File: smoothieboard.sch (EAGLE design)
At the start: 237 parts, among them IC1 LPC1769, IC10 LM1117-3.3V, IC11 78L12F, IC2 A4982, IC3 A4982, IC4 MCP44X1, IC5 A4982, IC6 A4982, J10 POWER_JACKSMD, J5 POWER_JACKSMD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

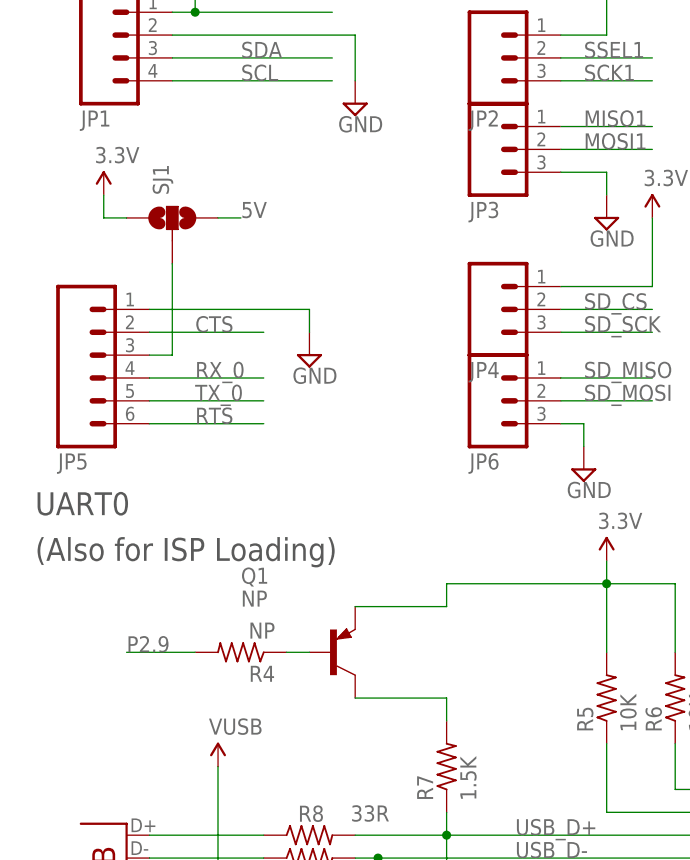
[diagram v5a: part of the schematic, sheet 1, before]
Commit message: switch USB CONNECT transistor for a FET, move UART voltage selector next to UART header
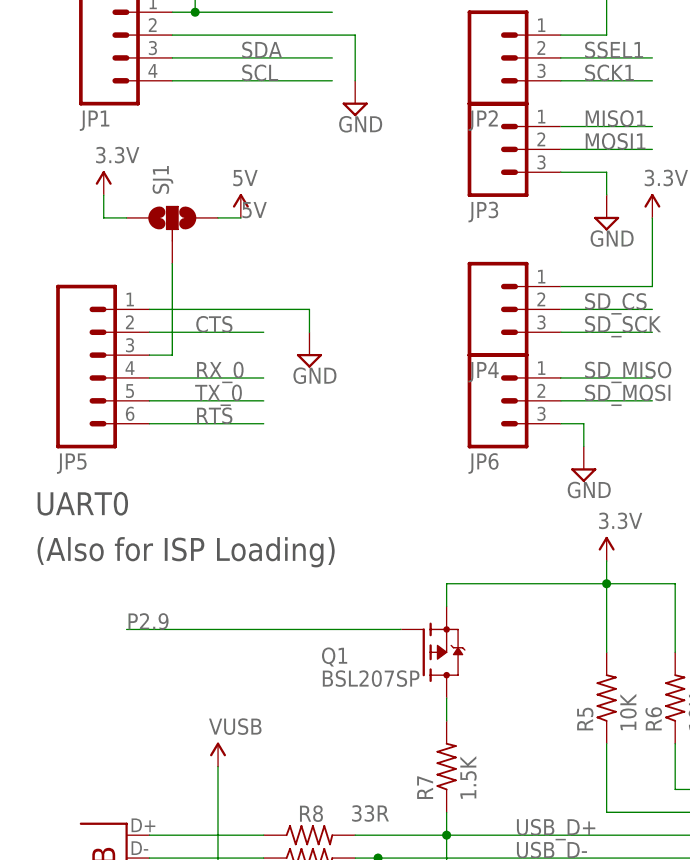
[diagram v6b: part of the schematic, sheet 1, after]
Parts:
- removed R4: NP, resistor:R-US_R0603
- Q1: value NP -> BSL207SP; device transistor-pnp:BC857ALT1SMD -> transistor-fet:BSL207SP
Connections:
- removed net N$59: Q1.B, R4.1
- net 3.3V: now also Q1.S; no longer Q1.E
- net N$51: now also Q1.D; no longer Q1.C
- net P2.9: now also Q1.G; no longer R4.2
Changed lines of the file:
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@@
 <part name="R57" library="resistor" deviceset="R-US_" device="R0603" value="49.9R"/>
 <part name="JP20" library="SparkFun" deviceset="M03" device="PTH"/>
-<part name="Q1" library="transistor-pnp" deviceset="BC857*" device="SMD" technology="ALT1" value="NP"/>
-<part name="R4" library="resistor" deviceset="R-US_" device="R0603" value="NP"/>
 <part name="JP13" library="SparkFun" deviceset="M04" device="1X04_NO_SILK"/>
 <part name="SUPPLY71" library="supply2" deviceset="GND" device=""/>
@@
 <part name="SJ1" library="SparkFun" deviceset="SOLDERJUMPER_2WAY" device="S"/>
 <part name="P+23" library="SparkFun" deviceset="3.3V" device=""/>
+<part name="Q1" library="transistor-fet" deviceset="BSL207SP" device=""/>
+<part name="U$3" library="SparkFun" deviceset="5V" device=""/>
+<part name="U$4" library="SparkFun" deviceset="5V" device=""/>
 </parts>
 <sheets>
@@
 <instance part="SUPPLY36" gate="GND" x="73.66" y="193.04"/>
 <instance part="JP20" gate="G$1" x="378.46" y="88.9" rot="R180"/>
-<instance part="Q1" gate="G$1" x="45.72" y="172.72"/>
-<instance part="R4" gate="G$1" x="35.56" y="172.72" rot="R180"/>
 <instance part="JP13" gate="G$1" x="375.92" y="132.08" rot="R180"/>
 <instance part="SUPPLY74" gate="GND" x="281.94" y="119.38" rot="R270"/>
@@
 <instance part="SJ1" gate="G$1" x="27.94" y="220.98" rot="R90"/>
 <instance part="P+23" gate="G$1" x="20.32" y="223.52"/>
+<instance part="Q1" gate="G$1" x="55.88" y="172.72"/>
+<instance part="U$4" gate="G$1" x="35.56" y="220.98"/>
 </instances>
 <busses>
@@
 <pinref part="P+30" gate="G$1" pin="3.3V"/>
 <pinref part="R6" gate="G$1" pin="2"/>
-<pinref part="Q1" gate="G$1" pin="E"/>
 <wire x1="58.42" y1="177.8" x2="58.42" y2="180.34" width="0.1524" layer="91"/>
 <wire x1="58.42" y1="180.34" x2="76.2" y2="180.34" width="0.1524" layer="91"/>
-<wire x1="58.42" y1="177.8" x2="48.26" y2="177.8" width="0.1524" layer="91"/>
+<pinref part="Q1" gate="G$1" pin="S"/>
 </segment>
 <segment>
@@
 </segment>
 <segment>
-<pinref part="SJ1" gate="G$1" pin="1"/>
 <pinref part="P+23" gate="G$1" pin="3.3V"/>
-<wire x1="22.86" y1="220.98" x2="20.32" y2="220.98" width="0.1524" layer="91"/>
 <wire x1="20.32" y1="220.98" x2="20.32" y2="223.52" width="0.1524" layer="91"/>
+<pinref part="SJ1" gate="G$1" pin="1"/>
+<wire x1="20.32" y1="220.98" x2="22.86" y2="220.98" width="0.1524" layer="91"/>
 </segment>
 </net>
@@
 </segment>
 <segment>
-<pinref part="R4" gate="G$1" pin="2"/>
-<wire x1="30.48" y1="172.72" x2="22.86" y2="172.72" width="0.1524" layer="91"/>
-<label x="22.86" y="172.72" size="1.778" layer="95"/>
+<wire x1="53.34" y1="175.26" x2="22.86" y2="175.26" width="0.1524" layer="91"/>
+<label x="22.86" y="175.26" size="1.778" layer="95"/>
+<pinref part="Q1" gate="G$1" pin="G"/>
 </segment>
 </net>
@@
 <net name="5V" class="0">
 <segment>
+<pinref part="U$4" gate="G$1" pin="5V"/>
+<pinref part="SJ1" gate="G$1" pin="3"/>
 <wire x1="33.02" y1="220.98" x2="35.56" y2="220.98" width="0.1524" layer="91"/>
 <label x="35.56" y="220.98" size="1.778" layer="95"/>
-<pinref part="SJ1" gate="G$1" pin="3"/>
 </segment>
 </net>
 <net name="N$51" class="0">
 <segment>
-<pinref part="Q1" gate="G$1" pin="C"/>
 <pinref part="R7" gate="G$1" pin="2"/>
 <wire x1="58.42" y1="167.64" x2="58.42" y2="165.1" width="0.1524" layer="91"/>
-<wire x1="58.42" y1="167.64" x2="48.26" y2="167.64" width="0.1524" layer="91"/>
-</segment>
-</net>
-<net name="N$59" class="0">
-<segment>
-<pinref part="Q1" gate="G$1" pin="B"/>
-<pinref part="R4" gate="G$1" pin="1"/>
-<wire x1="40.64" y1="172.72" x2="43.18" y2="172.72" width="0.1524" layer="91"/>
+<pinref part="Q1" gate="G$1" pin="D"/>
 </segment>
 </net>
@@
 <segment>
 <pinref part="JP5" gate="G$1" pin="3"/>
-<pinref part="SJ1" gate="G$1" pin="2"/>
 <wire x1="25.4" y1="205.74" x2="27.94" y2="205.74" width="0.1524" layer="91"/>
 <wire x1="27.94" y1="205.74" x2="27.94" y2="215.9" width="0.1524" layer="91"/>
+<pinref part="SJ1" gate="G$1" pin="2"/>
 </segment>
 </net>
@@
 <instance part="U$2" gate="B" x="162.56" y="86.36"/>
 <instance part="IC11" gate="G$1" x="170.18" y="142.24"/>
+<instance part="U$3" gate="G$1" x="43.18" y="38.1"/>
 </instances>
 <busses>
@@
 <segment>
 <wire x1="35.56" y1="48.26" x2="35.56" y2="38.1" width="0.1524" layer="91"/>
-<wire x1="35.56" y1="38.1" x2="45.72" y2="38.1" width="0.1524" layer="91"/>
+<wire x1="35.56" y1="38.1" x2="43.18" y2="38.1" width="0.1524" layer="91"/>
+<wire x1="43.18" y1="38.1" x2="45.72" y2="38.1" width="0.1524" layer="91"/>
 <wire x1="35.56" y1="33.02" x2="35.56" y2="38.1" width="0.1524" layer="91"/>
 <wire x1="33.02" y1="38.1" x2="35.56" y2="38.1" width="0.1524" layer="91"/>
@@
 <pinref part="D1" gate="G$1" pin="C"/>
 <pinref part="D2" gate="G$1" pin="C"/>
+<pinref part="U$3" gate="G$1" pin="5V"/>
+<junction x="43.18" y="38.1"/>
 </segment>
 </net>

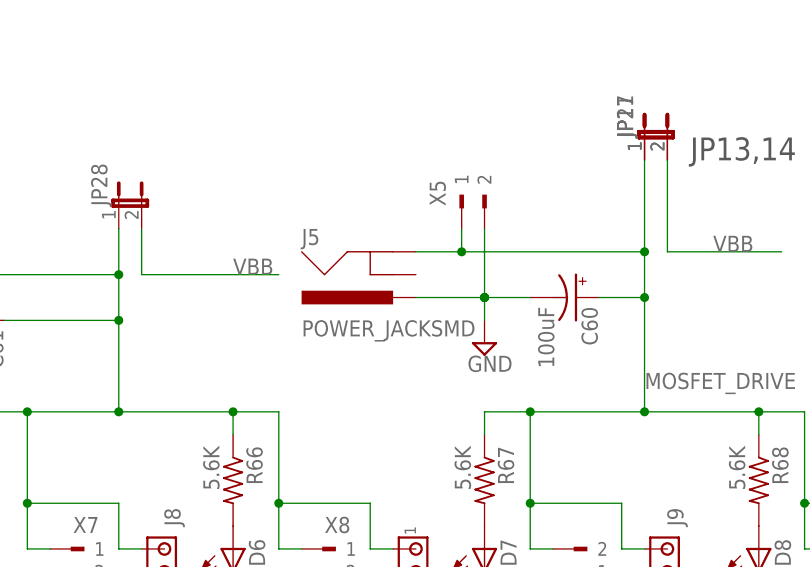
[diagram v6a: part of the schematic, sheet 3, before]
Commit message: Removed Mosfet Driver Power SMD Jack
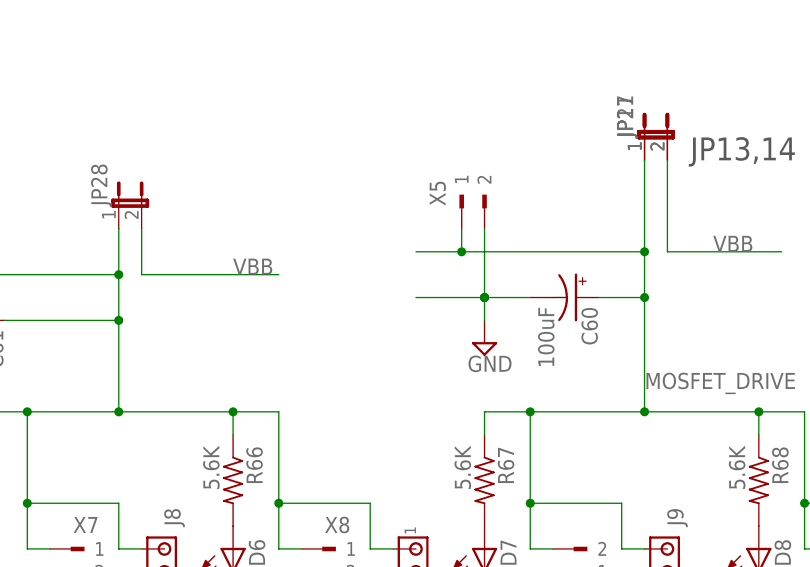
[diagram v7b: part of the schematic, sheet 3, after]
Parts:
- removed J5: POWER_JACKSMD, SparkFun:POWER_JACKSMD
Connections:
- net GND: no longer J5.PWR
- net MOSFET_DRIVE: no longer J5.GND
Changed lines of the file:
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@@
 <grid distance="0.1" unitdist="inch" unit="inch" style="lines" multiple="1" display="no" altdistance="0.01" altunitdist="inch" altunit="inch"/>
 <layers>
-<layer number="1" name="Top" color="4" fill="1" visible="yes" active="no"/>
-<layer number="2" name="Route2" color="2" fill="1" visible="yes" active="no"/>
-<layer number="3" name="Route3" color="4" fill="3" visible="yes" active="no"/>
-<layer number="4" name="Route4" color="1" fill="4" visible="yes" active="no"/>
-<layer number="5" name="Route5" color="4" fill="4" visible="yes" active="no"/>
-<layer number="6" name="Route6" color="1" fill="8" visible="yes" active="no"/>
-<layer number="7" name="Route7" color="4" fill="8" visible="yes" active="no"/>
-<layer number="8" name="Route8" color="1" fill="2" visible="yes" active="no"/>
-<layer number="9" name="Route9" color="4" fill="2" visible="yes" active="no"/>
-<layer number="10" name="Route10" color="1" fill="7" visible="yes" active="no"/>
-<layer number="11" name="Route11" color="4" fill="7" visible="yes" active="no"/>
-<layer number="12" name="Route12" color="1" fill="5" visible="yes" active="no"/>
-<layer number="13" name="Route13" color="4" fill="5" visible="yes" active="no"/>
-<layer number="14" name="Route14" color="1" fill="6" visible="yes" active="no"/>
-<layer number="15" name="Route15" color="5" fill="1" visible="yes" active="no"/>
-<layer number="16" name="Bottom" color="1" fill="1" visible="yes" active="no"/>
-<layer number="17" name="Pads" color="2" fill="1" visible="yes" active="no"/>
-<layer number="18" name="Vias" color="2" fill="1" visible="yes" active="no"/>
-<layer number="19" name="Unrouted" color="6" fill="1" visible="yes" active="no"/>
-<layer number="20" name="Dimension" color="15" fill="1" visible="yes" active="no"/>
-<layer number="21" name="tPlace" color="7" fill="1" visible="yes" active="no"/>
-<layer number="22" name="bPlace" color="7" fill="1" visible="yes" active="no"/>
-<layer number="23" name="tOrigins" color="15" fill="1" visible="yes" active="no"/>
-<layer number="24" name="bOrigins" color="15" fill="1" visible="yes" active="no"/>
-<layer number="25" name="tNames" color="7" fill="1" visible="yes" active="no"/>
-<layer number="26" name="bNames" color="7" fill="1" visible="yes" active="no"/>
-<layer number="27" name="tValues" color="7" fill="1" visible="yes" active="no"/>
-<layer number="28" name="bValues" color="7" fill="1" visible="yes" active="no"/>
+<layer number="1" name="Top" color="4" fill="1" visible="no" active="no"/>
+<layer number="2" name="Route2" color="2" fill="1" visible="no" active="no"/>
+<layer number="3" name="Route3" color="4" fill="3" visible="no" active="no"/>
+<layer number="4" name="Route4" color="1" fill="4" visible="no" active="no"/>
+<layer number="5" name="Route5" color="4" fill="4" visible="no" active="no"/>
+<layer number="6" name="Route6" color="1" fill="8" visible="no" active="no"/>
+<layer number="7" name="Route7" color="4" fill="8" visible="no" active="no"/>
+<layer number="8" name="Route8" color="1" fill="2" visible="no" active="no"/>
+<layer number="9" name="Route9" color="4" fill="2" visible="no" active="no"/>
+<layer number="10" name="Route10" color="1" fill="7" visible="no" active="no"/>
+<layer number="11" name="Route11" color="4" fill="7" visible="no" active="no"/>
+<layer number="12" name="Route12" color="1" fill="5" visible="no" active="no"/>
+<layer number="13" name="Route13" color="4" fill="5" visible="no" active="no"/>
+<layer number="14" name="Route14" color="1" fill="6" visible="no" active="no"/>
+<layer number="15" name="Route15" color="5" fill="1" visible="no" active="no"/>
+<layer number="16" name="Bottom" color="1" fill="1" visible="no" active="no"/>
+<layer number="17" name="Pads" color="2" fill="1" visible="no" active="no"/>
+<layer number="18" name="Vias" color="2" fill="1" visible="no" active="no"/>
+<layer number="19" name="Unrouted" color="6" fill="1" visible="no" active="no"/>
+<layer number="20" name="Dimension" color="15" fill="1" visible="no" active="no"/>
+<layer number="21" name="tPlace" color="7" fill="1" visible="no" active="no"/>
+<layer number="22" name="bPlace" color="7" fill="1" visible="no" active="no"/>
+<layer number="23" name="tOrigins" color="15" fill="1" visible="no" active="no"/>
+<layer number="24" name="bOrigins" color="15" fill="1" visible="no" active="no"/>
+<layer number="25" name="tNames" color="7" fill="1" visible="no" active="no"/>
+<layer number="26" name="bNames" color="7" fill="1" visible="no" active="no"/>
+<layer number="27" name="tValues" color="7" fill="1" visible="no" active="no"/>
+<layer number="28" name="bValues" color="7" fill="1" visible="no" active="no"/>
 <layer number="29" name="tStop" color="7" fill="3" visible="no" active="no"/>
 <layer number="30" name="bStop" color="7" fill="6" visible="no" active="no"/>
@@
 <layer number="35" name="tGlue" color="7" fill="4" visible="no" active="no"/>
 <layer number="36" name="bGlue" color="7" fill="5" visible="no" active="no"/>
-<layer number="37" name="tTest" color="7" fill="1" visible="yes" active="no"/>
-<layer number="38" name="bTest" color="7" fill="1" visible="yes" active="no"/>
+<layer number="37" name="tTest" color="7" fill="1" visible="no" active="no"/>
+<layer number="38" name="bTest" color="7" fill="1" visible="no" active="no"/>
 <layer number="39" name="tKeepout" color="4" fill="11" visible="no" active="no"/>
 <layer number="40" name="bKeepout" color="1" fill="11" visible="no" active="no"/>
@@
 <layer number="44" name="Drills" color="7" fill="1" visible="no" active="no"/>
 <layer number="45" name="Holes" color="7" fill="1" visible="no" active="no"/>
-<layer number="46" name="Milling" color="3" fill="1" visible="yes" active="no"/>
-<layer number="47" name="Measures" color="7" fill="1" visible="yes" active="no"/>
-<layer number="48" name="Document" color="7" fill="1" visible="yes" active="no"/>
-<layer number="49" name="Reference" color="7" fill="1" visible="yes" active="no"/>
-<layer number="50" name="dxf" color="7" fill="1" visible="yes" active="no"/>
-<layer number="51" name="tDocu" color="7" fill="1" visible="yes" active="no"/>
-<layer number="52" name="bDocu" color="7" fill="1" visible="yes" active="no"/>
-<layer number="53" name="tGND_GNDA" color="7" fill="9" visible="yes" active="no"/>
-<layer number="54" name="bGND_GNDA" color="1" fill="9" visible="yes" active="no"/>
-<layer number="56" name="wert" color="7" fill="1" visible="yes" active="no"/>
+<layer number="46" name="Milling" color="3" fill="1" visible="no" active="no"/>
+<layer number="47" name="Measures" color="7" fill="1" visible="no" active="no"/>
+<layer number="48" name="Document" color="7" fill="1" visible="no" active="no"/>
+<layer number="49" name="Reference" color="7" fill="1" visible="no" active="no"/>
+<layer number="50" name="dxf" color="7" fill="1" visible="no" active="no"/>
+<layer number="51" name="tDocu" color="7" fill="1" visible="no" active="no"/>
+<layer number="52" name="bDocu" color="7" fill="1" visible="no" active="no"/>
+<layer number="53" name="tGND_GNDA" color="7" fill="9" visible="no" active="no"/>
+<layer number="54" name="bGND_GNDA" color="1" fill="9" visible="no" active="no"/>
+<layer number="56" name="wert" color="7" fill="1" visible="no" active="no"/>
 <layer number="91" name="Nets" color="2" fill="1" visible="yes" active="yes"/>
 <layer number="92" name="Busses" color="1" fill="1" visible="yes" active="yes"/>
@@
 <part name="C63" library="SparkFun" deviceset="CAP_POL" device="D" value="100uF"/>
 <part name="J10" library="SparkFun" deviceset="POWER_JACK" device="SMD"/>
-<part name="J5" library="SparkFun" deviceset="POWER_JACK" device="SMD"/>
 <part name="X12" library="con-weidmueller-sl35" deviceset="180G-2" device=""/>
 <part name="X11" library="con-weidmueller-sl35" deviceset="180G-2" device=""/>
@@
 <instance part="C63" gate="G$1" x="175.26" y="33.02"/>
 <instance part="J10" gate="G$1" x="119.38" y="45.72" rot="MR180"/>
-<instance part="J5" gate="G$1" x="284.48" y="127" rot="MR180"/>
 <instance part="X12" gate="G$1" x="15.24" y="38.1" rot="R180"/>
 <instance part="X11" gate="G$1" x="124.46" y="50.8" rot="R90"/>
@@
 <pinref part="SUPPLY24" gate="GND" pin="GND"/>
 <pinref part="C60" gate="G$1" pin="-"/>
-<pinref part="J5" gate="G$1" pin="PWR"/>
 <pinref part="X5" gate="G$1" pin="2"/>
 </segment>
@@
 <pinref part="C60" gate="G$1" pin="+"/>
 <pinref part="X9" gate="G$1" pin="1"/>
-<pinref part="J5" gate="G$1" pin="GND"/>
 <pinref part="X5" gate="G$1" pin="1"/>
 <pinref part="JP11" gate="A" pin="1"/>
